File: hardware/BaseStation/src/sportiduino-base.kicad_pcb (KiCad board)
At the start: 2 copper layers, 76.8 x 44.7 mm, 40 parts, among them SW1 SW_Reed, X1 Battery, X2 Prog, X3 RC522

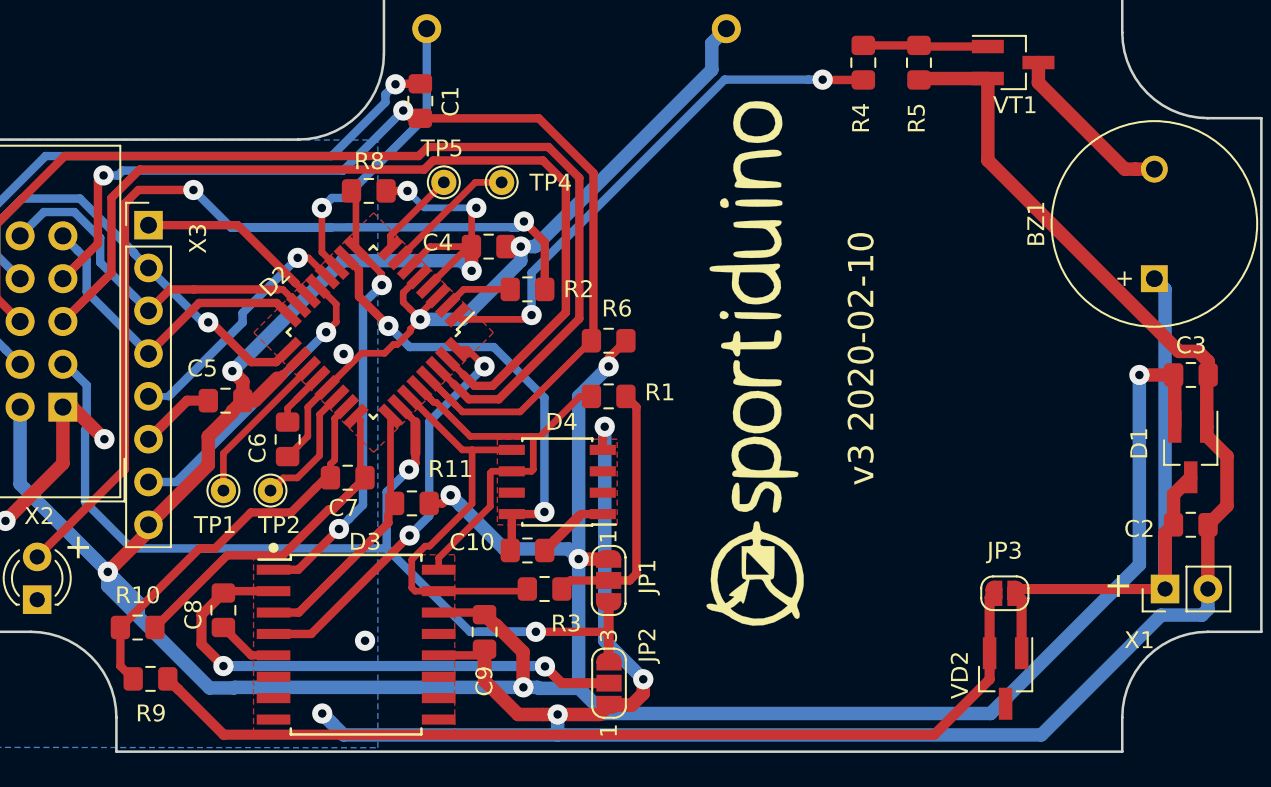
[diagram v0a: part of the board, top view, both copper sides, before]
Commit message: BS PCB v3 2020-03-23: removed dual diode VD2 from measurement circuit
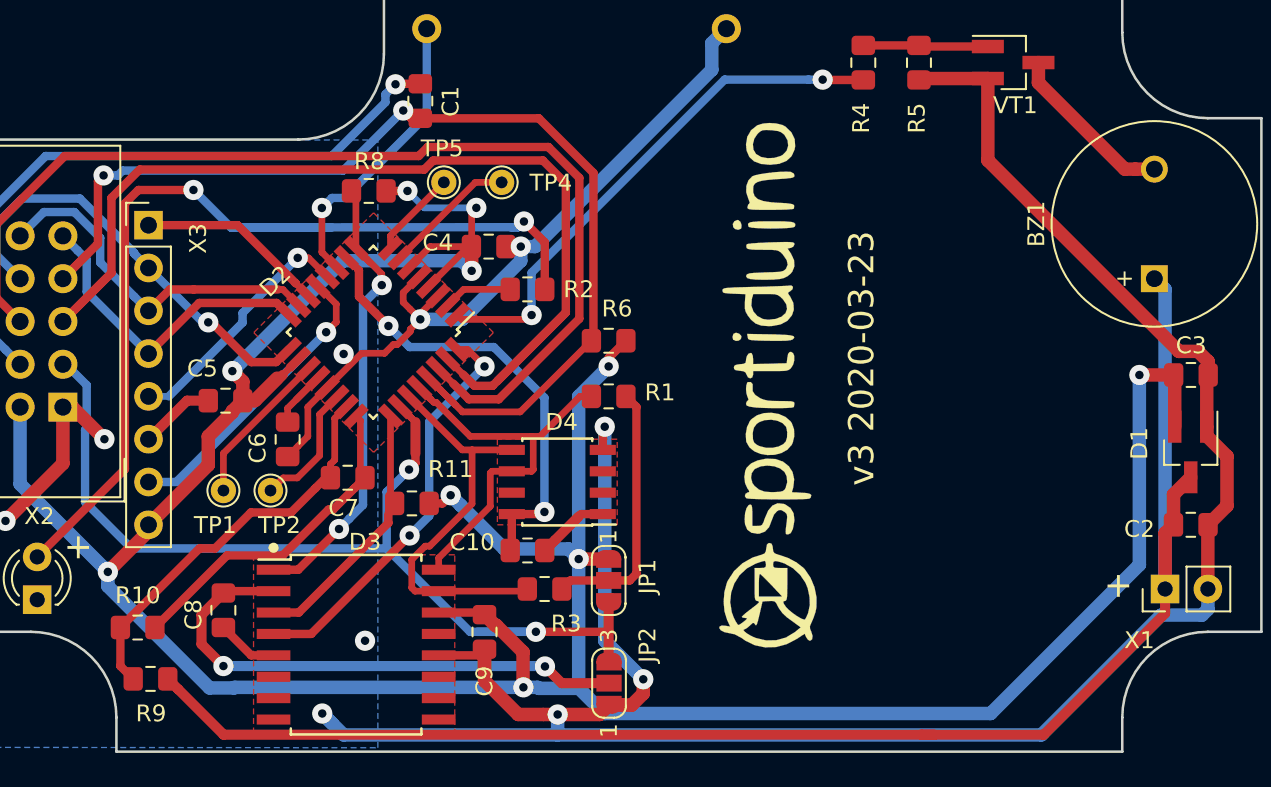
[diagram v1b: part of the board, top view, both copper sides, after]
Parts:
- removed JP3: SolderJumper_2_Open, Jumper:SolderJumper-2_P1.3mm_Open_RoundedPad1.0x1.5mm
- removed VD2: BAV99, Package_TO_SOT_SMD:SOT-23_Handsoldering
- moved G*** 1.50 mm to (181.4, 81.5)
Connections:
- R9 pad 2: Net-(JP3-Pad2) -> +BATT
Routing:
- net Net-(JP3-Pad2): track 57.3 -> 0.00 mm
- net +BATT: track 38.6 -> 91.7 mm
- net +3V3: track 205.6 -> 202.4 mm
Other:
- board text added: "v3 2020-03-23"
- board text removed: "v3 2020-02-10"

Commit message: New PCB (WiP)
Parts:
- removed JP2: SolderJumper_3_Bridged12, Jumper:SolderJumper-3_P1.3mm_Open_RoundedPad1.0x1.5mm_NumberLabels
- X1: footprint Connector_PinHeader_2.54mm:PinHeader_1x02_P2.54mm_Vertical -> Connector_JST:JST_XH_B2B-XH-A_1x02_P2.50mm_Vertical
- X2: footprint Connector_IDC:IDC-Header_2x05_P2.54mm_Vertical -> Connector_PinHeader_2.54mm:PinHeader_2x04_P2.54mm_Vertical
- X3: moved to B.Cu
- moved TP5 74.7 mm to (168.0, 144.0)
- moved TP4 74.4 mm to (164.0, 144.0)
- moved TP2 56.7 mm to (160.0, 144.0)
- moved JP1 56.7 mm to (115.3, 96.0), turned to 0 degrees
- moved TP1 56.6 mm to (156.0, 144.0)
- moved C1 52.6 mm to (109.0, 73.7)
- moved G*** 47.0 mm to (166.9, 36.8)
- moved C6 44.9 mm to (121.9, 117.3)
- moved R1 44.6 mm to (185.7, 124.7)
- moved R6 41.2 mm to (188.7, 116.6)
- moved R2 38.9 mm to (188.0, 108.7)
- moved C4 37.9 mm to (180.8, 107.7)
- moved C9 35.4 mm to (150.1, 128.5)
- moved D4 35.2 mm to (171.7, 122.4)
- moved C2 33.0 mm to (239.5, 88.9)
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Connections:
- D3 pad 2: Net-(C8-Pad1) -> GNDD
- JP1 pad 1: +3V3 -> Net-(JP1-Pad1)
- JP1 pad 3: PC3 -> Net-(JP1-Pad3)
- R1 pad 1: Net-(JP1-Pad2) -> +3V3
- R3 pad 1: Net-(JP1-Pad2) -> +3V3
- X1 pad 1: +BATT -> GNDD
- X1 pad 2: GNDD -> +BATT
- X3 pad 1: /PB2 -> +3V3
- X3 pad 2: PB5 -> /PB1
- X3 pad 3: PB3 -> GNDD
- X3 pad 4: PB4 -> /PB0
- X3 pad 5: /PB0 -> PB4
- X3 pad 6: GNDD -> PB3
- X3 pad 7: /PB1 -> PB5
- X3 pad 8: +3V3 -> /PB2
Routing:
- net GNDD: track 205.1 -> 0.00 mm, vias 10 -> 0
- net +3V3: track 202.4 -> 0.00 mm, vias 10 -> 0
- net +BATT: track 91.7 -> 0.00 mm
- net TX: track 69.9 -> 0.00 mm
- net RST: track 66.1 -> 0.00 mm, vias 2 -> 0
- net RX: track 63.1 -> 0.00 mm
- net PC3: track 60.6 -> 0.00 mm, vias 2 -> 0
- net Net-(R2-Pad1): track 59.5 -> 0.00 mm, vias 2 -> 0
- net Net-(C1-Pad2): track 39.1 -> 0.00 mm, vias 1 -> 0
- net Net-(C8-Pad1): track 31.7 -> 0.00 mm, vias 2 -> 0
- net /BUZ: track 31.6 -> 0.00 mm, vias 2 -> 0
- net PD6: track 28.1 -> 0.00 mm, vias 2 -> 0
- net 32K: track 27.9 -> 0.00 mm, vias 2 -> 0
- net PB5: track 27.1 -> 0.00 mm, vias 1 -> 0
- net /SCL: track 25.0 -> 0.00 mm
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- removed copper zone on B.Cu, net GNDD
- removed copper zone on F.Cu, net GNDD
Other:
- board size 76.8 x 44.7 mm -> 73 x 44 mm
- board text removed: "RC522"
